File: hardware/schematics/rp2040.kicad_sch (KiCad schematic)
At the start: 27 parts, among them SW1 TS-1088-AR02016, U1 RP2040, U2 W25Q128JVSIQTR, X1 X322512MSB4SI

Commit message: Arrange components
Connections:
- net +1V1 renamed 1.1V
- net +3.3V renamed 3.3V
- net +5V renamed 5V

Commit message: Add more routing
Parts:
- removed R6, R7: 5k1, Resistor_SMD:R_0603_1608Metric, symbol Device:R
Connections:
- net 5V: no longer names the net of USB1.11 (VBUS)
- net 5V: no longer USB1.2 (VBUS)

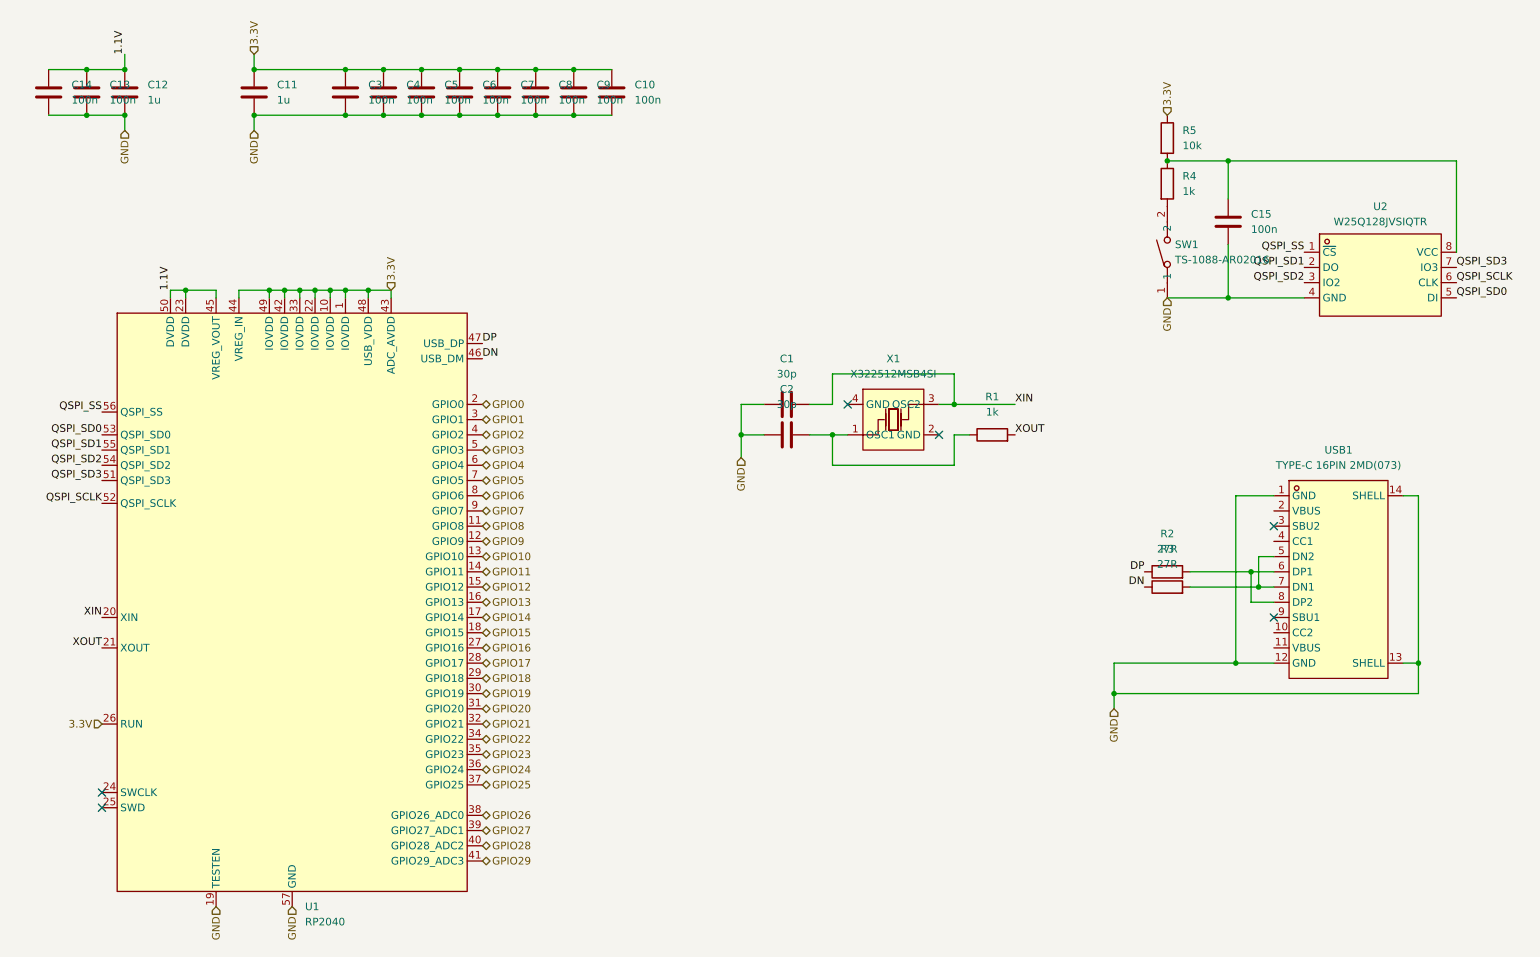
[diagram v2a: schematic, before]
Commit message: Fix BOOTSEL resistors and add reset button
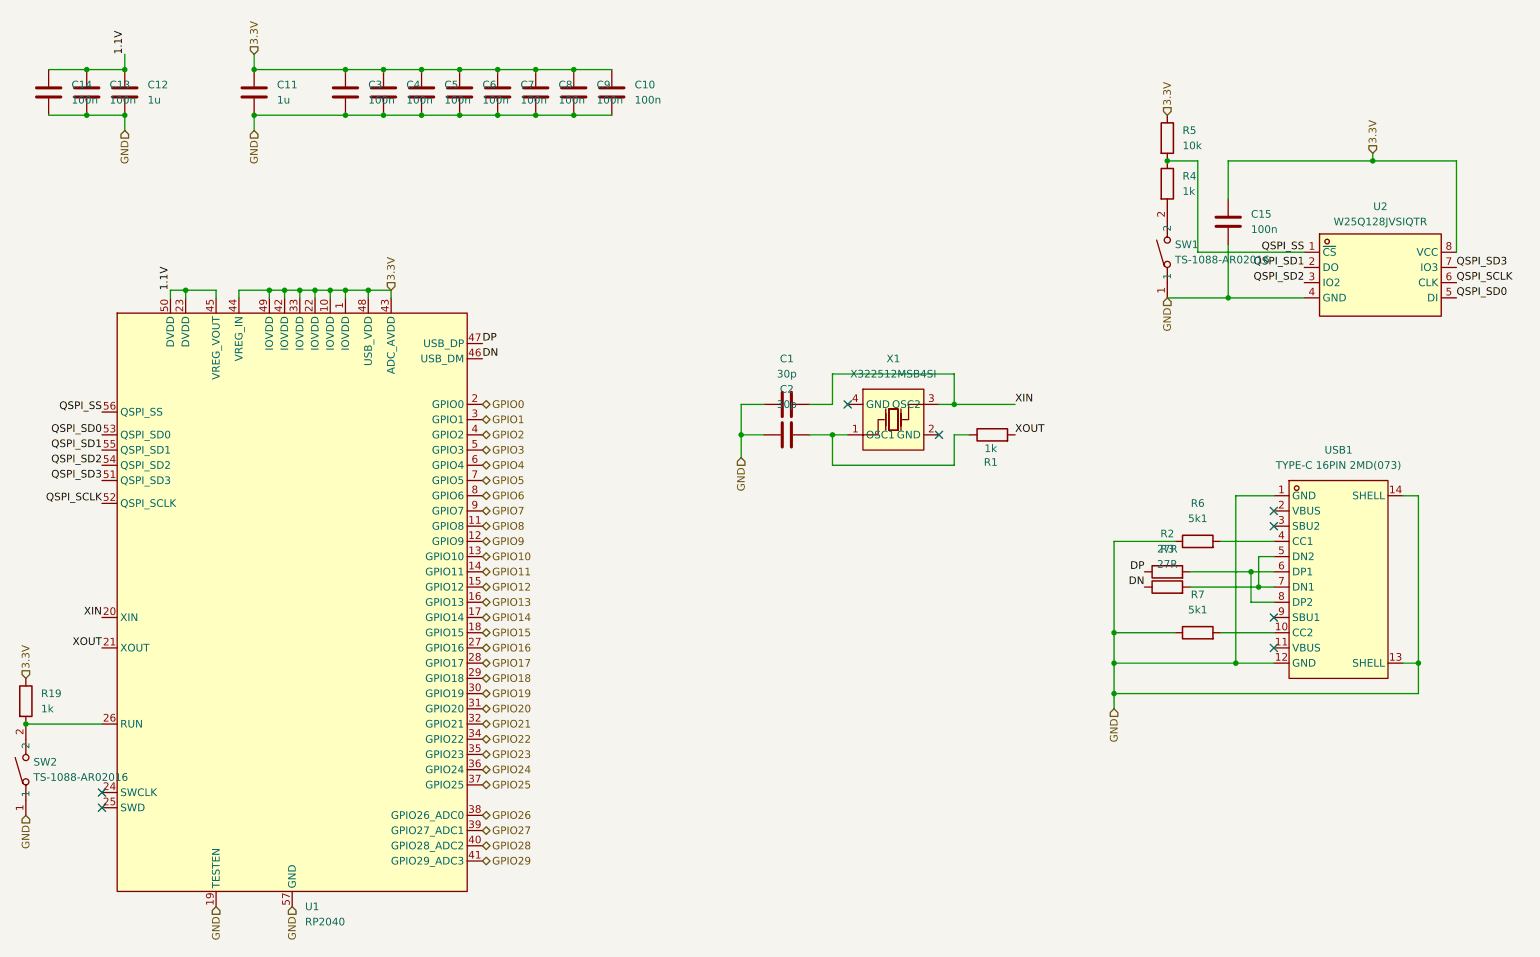
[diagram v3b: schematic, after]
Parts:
- added R19: 1k, Resistor_SMD:R_0603_1608Metric, symbol Device:R
- added R6, R7: 5k1, Resistor_SMD:R_0603_1608Metric, symbol Device:R
- added SW2: TS-1088-AR02016, easyeda2kicad:SW-SMD_L3.9-W3.0-P4.45, symbol easyeda2kicad:TS-1088-AR02016
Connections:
- net 3.3V: now also C15.1, U2.8 (VCC), R19.1; no longer U1.26 (RUN)
- net GND: now also R6.1, R7.1, SW2.1
- net QSPI_SS: now also R4.1, R5.2
- net at USB1.10 (CC2): now also R7.2
- net at USB1.4 (CC1): now also R6.2
- new net: R19.2, SW2.2, U1.26 (RUN)
- no-connect marks 6 -> 8

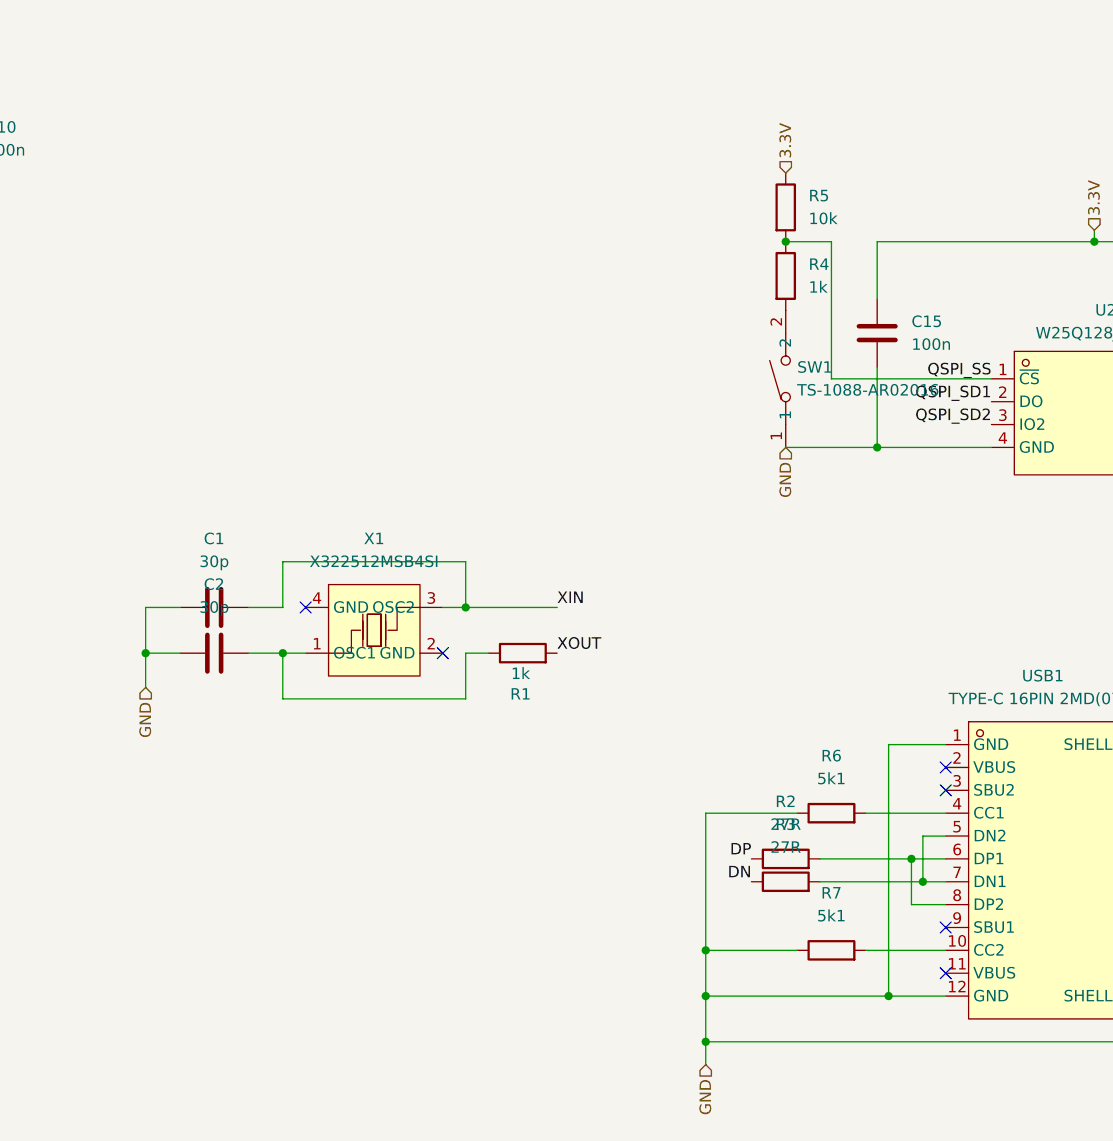
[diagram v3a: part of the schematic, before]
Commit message: Change logic supply to come from VBUS
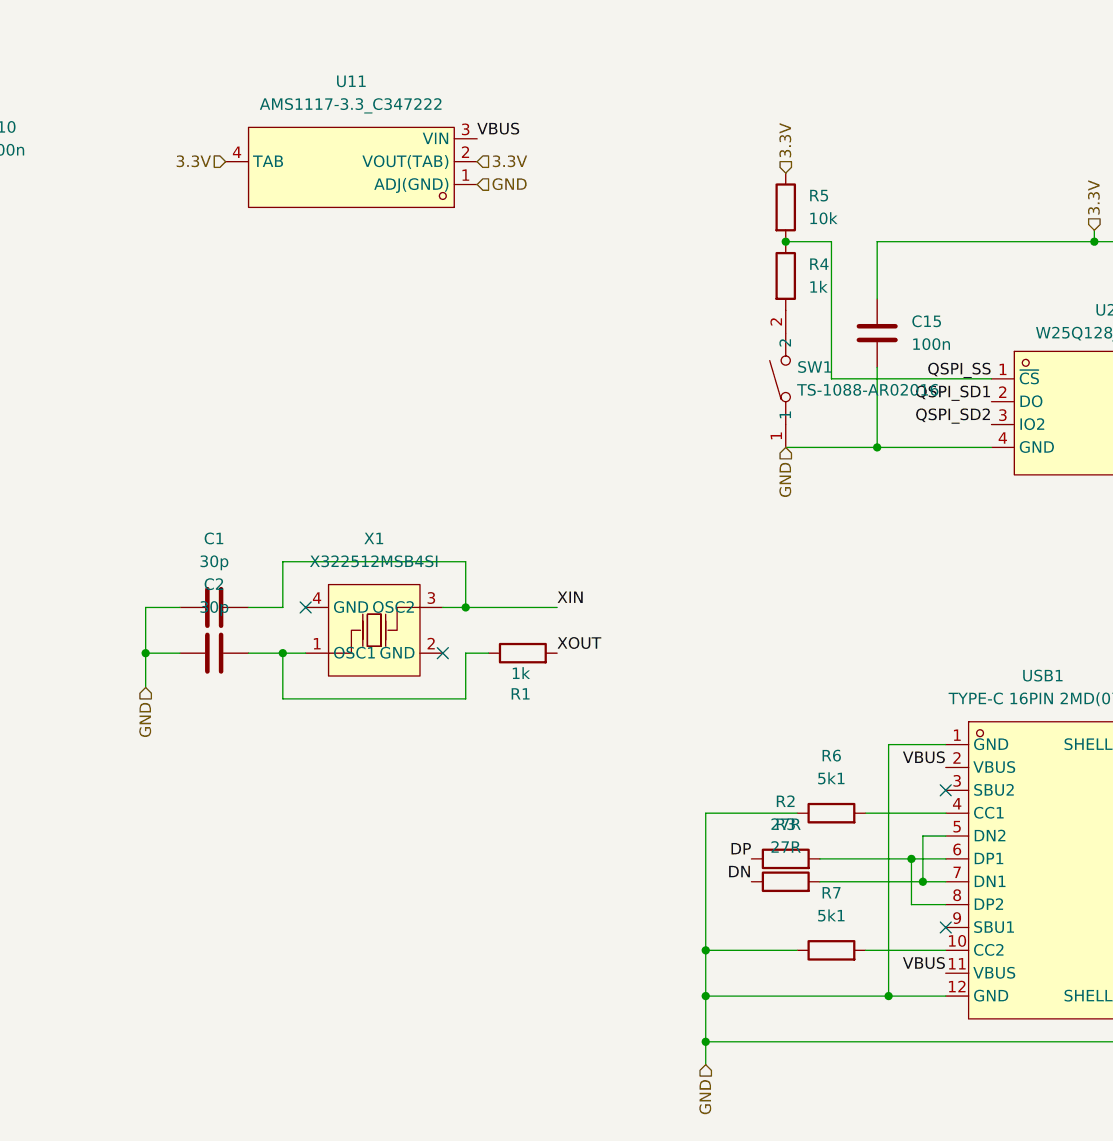
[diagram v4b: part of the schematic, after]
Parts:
- added U11: AMS1117-3.3_C347222, easyeda2kicad:SOT-223-4_L6.5-W3.5-P2.30-LS7.0-BR, symbol easyeda2kicad:AMS1117-3.3_C347222
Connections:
- net 3.3V: now also U11.2 (VOUT(TAB)), U11.4 (TAB)
- net GND: now also U11.1 (ADJ(GND))
- net VBUS: now reaches USB1.11 (VBUS)
- net VBUS: now also USB1.2 (VBUS), U11.3 (VIN)
- no-connect marks 8 -> 6
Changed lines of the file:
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@@
 	)
 	(no_connect
-		(at 229.87 116.84)
-	)
-	(no_connect
 		(at 229.87 119.38)
 	)
@@
 	)
 	(no_connect
-		(at 229.87 139.7)
-	)
-	(no_connect
 		(at 158.75 99.06)
 	)
@@
 		)
 	)
+	(label "VBUS"
+		(at 229.87 139.7 180)
+		(effects
+			(font
+				(size 1.27 1.27)
+			)
+			(justify right bottom)
+		)
+	)
 	(label "1.1V"
 		(at 38.1 40.64 90)
@@
 		)
 	)
+	(label "VBUS"
+		(at 177.8 46.99 0)
+		(effects
+			(font
+				(size 1.27 1.27)
+			)
+			(justify left bottom)
+		)
+	)
 	(label "XIN"
 		(at 34.29 134.62 180)
@@
 		)
 	)
+	(label "VBUS"
+		(at 229.87 116.84 180)
+		(effects
+			(font
+				(size 1.27 1.27)
+			)
+			(justify right bottom)
+		)
+	)
 	(label "QSPI_SD2"
 		(at 234.95 78.74 180)
@@
 		)
 	)
+	(hierarchical_label "GND"
+		(shape input)
+		(at 177.8 52.07 0)
+		(effects
+			(font
+				(size 1.27 1.27)
+			)
+			(justify left)
+		)
+	)
 	(hierarchical_label "GPIO17"
 		(shape bidirectional)
@@
 		)
 	)
+	(hierarchical_label "3.3V"
+		(shape input)
+		(at 149.86 49.53 180)
+		(effects
+			(font
+				(size 1.27 1.27)
+			)
+			(justify right)
+		)
+	)
 	(hierarchical_label "GPIO18"
 		(shape bidirectional)
@@
 		)
 	)
+	(hierarchical_label "3.3V"
+		(shape input)
+		(at 177.8 49.53 0)
+		(effects
+			(font
+				(size 1.27 1.27)
+			)
+			(justify left)
+		)
+	)
 	(hierarchical_label "GND"
 		(shape input)
@@
 					(unit 1)
 				)
+			)
+		)
+	)
+	(symbol
+		(lib_id "easyeda2kicad:AMS1117-3.3_C347222")
+		(at 162.56 49.53 180)
+		(unit 1)
+		(exclude_from_sim no)
+		(in_bom yes)
+		(on_board yes)
+		(dnp no)
+		(fields_autoplaced yes)
+		(property "Reference" "U11"
+			(at 163.83 40.64 0)
+			(effects
+				(font
+					(size 1.27 1.27)
+				)
+			)
+		)
+		(property "Value" "AMS1117-3.3_C347222"
+			(at 163.83 43.18 0)
+			(effects
+				(font
+					(size 1.27 1.27)
+				)
+			)
+		)
+		(property "Footprint" "easyeda2kicad:SOT-223-4_L6.5-W3.5-P2.30-LS7.0-BR"
+			(at 162.56 39.37 0)
+			(effects
+				(font
+					(size 1.27 1.27)
+				)
+				(hide yes)
+			)
+		)
+		(property "Datasheet" "https://lcsc.com/product-detail/Others_Youtai-Semiconductor-Co-Ltd-AMS1117-3-3_C347222.html"
+			(at 162.56 36.83 0)
+			(effects
+				(font
+					(size 1.27 1.27)
+				)
+				(hide yes)
+			)
+		)
+		(property "Description" ""
+			(at 162.56 49.53 0)
+			(effects
+				(font
+					(size 1.27 1.27)
+				)
+				(hide yes)
+			)
+		)
+		(property "LCSC Part" "C347222"
+			(at 162.56 34.29 0)
+			(effects
+				(font
+					(size 1.27 1.27)
+				)
+				(hide yes)
+			)
+		)
+		(pin "4"
+		)
+		(pin "3"
+		)
+		(pin "2"
+		)
+		(pin "1"
+		)
+		(instances
+			(project "opentorque"
+				(path "/156c9497-a769-4db4-8dbf-f14841e5fc52/b3ea4619-d2c2-4d91-a61f-a64cab73bb7e"
+					(reference "U11")
+					(unit 1)
+				)

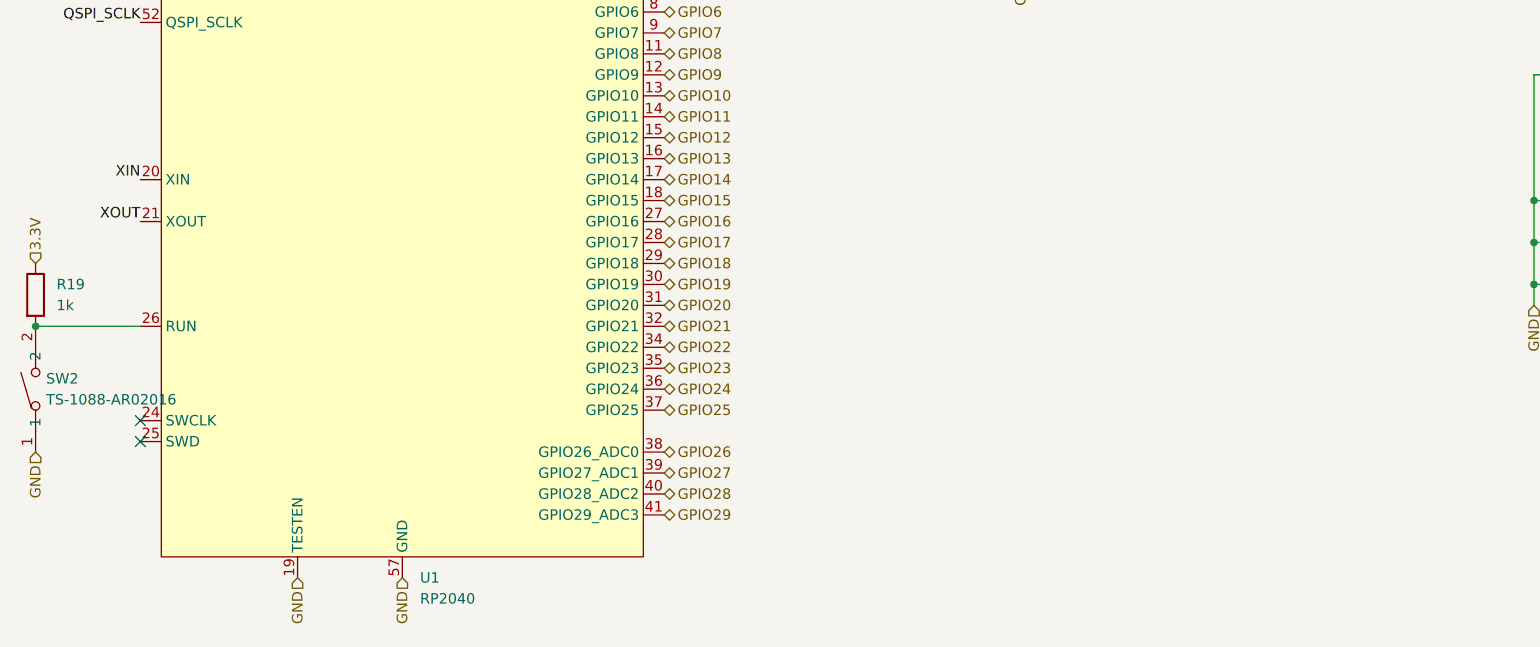
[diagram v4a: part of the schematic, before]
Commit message: Add LEDs and expand copper pours
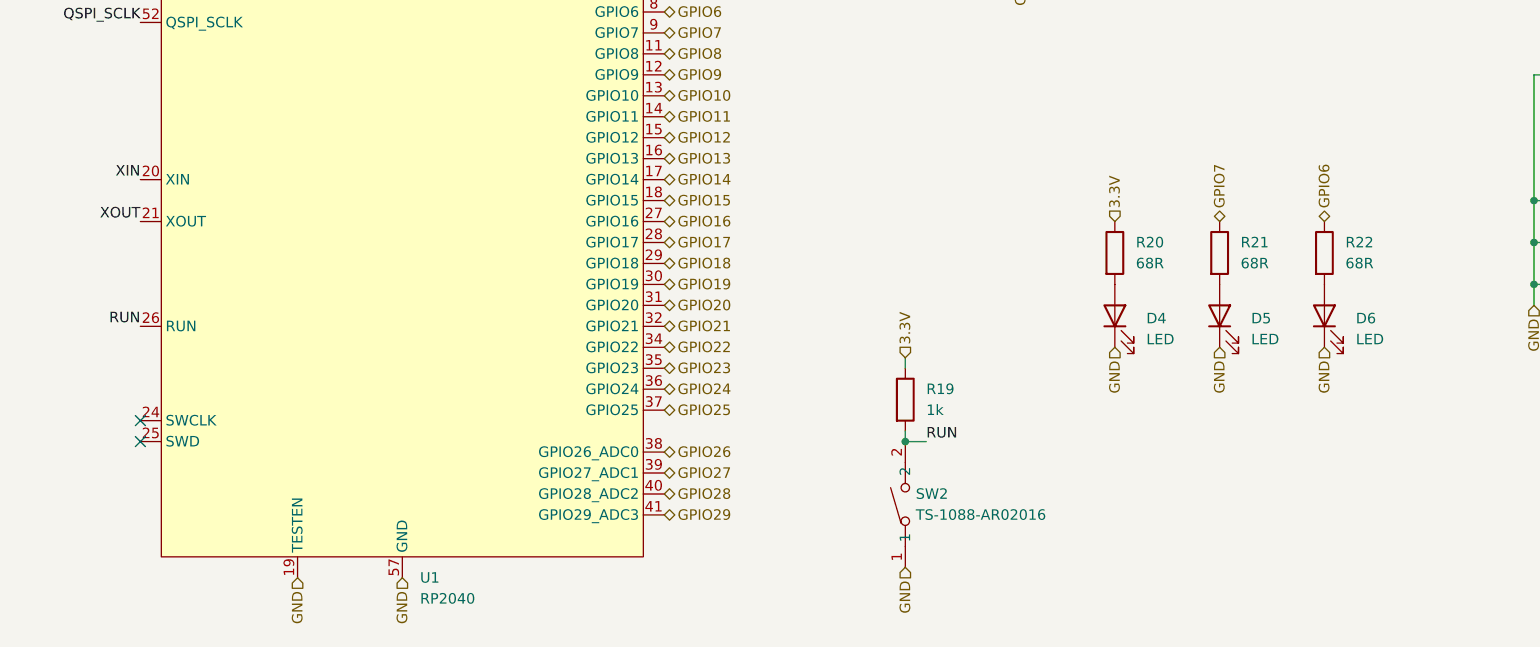
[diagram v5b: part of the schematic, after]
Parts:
- added D4, D5, D6: LED, LED_SMD:LED_0603_1608Metric, symbol Device:LED
- added R20, R21, R22: 68R, Resistor_SMD:R_0603_1608Metric, symbol Device:R
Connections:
- net 3.3V: now also R20.1
- net GND: now also D4.1 (K), D5.1 (K), D6.1 (K)
- net GPIO6: now also R22.1
- net GPIO7: now also R21.1
- net RUN: now reaches R19.2, SW2.2, U1.26 (RUN)
- new net: D6.2 (A), R22.2
- new net: D4.2 (A), R20.2
- new net: D5.2 (A), R21.2
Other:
- moved on the sheet: R19, SW2
